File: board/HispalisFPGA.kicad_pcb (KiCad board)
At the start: 4 copper layers, 91.3 x 79.9 mm, 133 parts, among them J1 HC-TYPE-C-16P-01A, Q1 DMG1012T, Q2 DMG1012T, Q3 DMG1012T, Q4 DMG1012T, SW1 SW_DIP_x08, U1 93LC46B, U2 FT2232HQ, Y1 12MHz

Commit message: Add metadata
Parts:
- moved BTN2 52.0 mm to (102.6, 105.6)
- moved C37 52.0 mm to (66.9, 101.7)
- moved C45 52.0 mm to (77.0, 97.5)
- moved DISPLAY1 52.0 mm to (62.7, 128.9)
- moved FLASH1 52.0 mm to (77.0, 97.5)
- moved FPGA1 52.0 mm to (62.5, 102.6)
- moved LD1 52.0 mm to (40.6, 136.1)
- moved LD2 52.0 mm to (45.6, 136.1)
- moved LD3 52.0 mm to (50.6, 136.1)
- moved LD4 52.0 mm to (55.6, 136.1)
- moved LD5 52.0 mm to (60.6, 136.1)
- moved LD6 52.0 mm to (65.6, 136.1)
- moved LD7 52.0 mm to (70.6, 136.1)
- moved LD8 52.0 mm to (75.6, 136.1)
- moved R1 52.0 mm to (92.1, 90.0)
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
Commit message: Add logo
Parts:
- added LOGO1: LOGO, HispalisFPGA:logo, F.Cu at (89.4, 76.8)

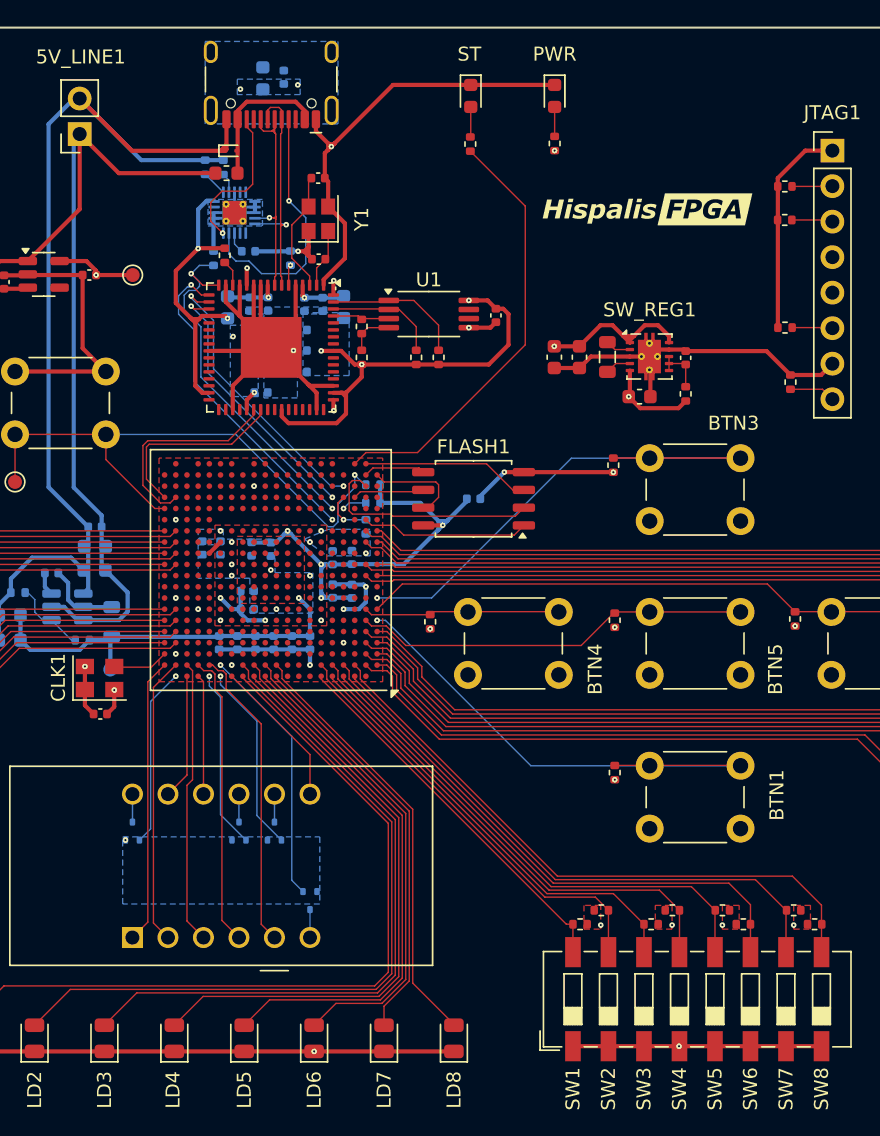
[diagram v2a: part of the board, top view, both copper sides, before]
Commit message: Further adaptations for JLCPCB order
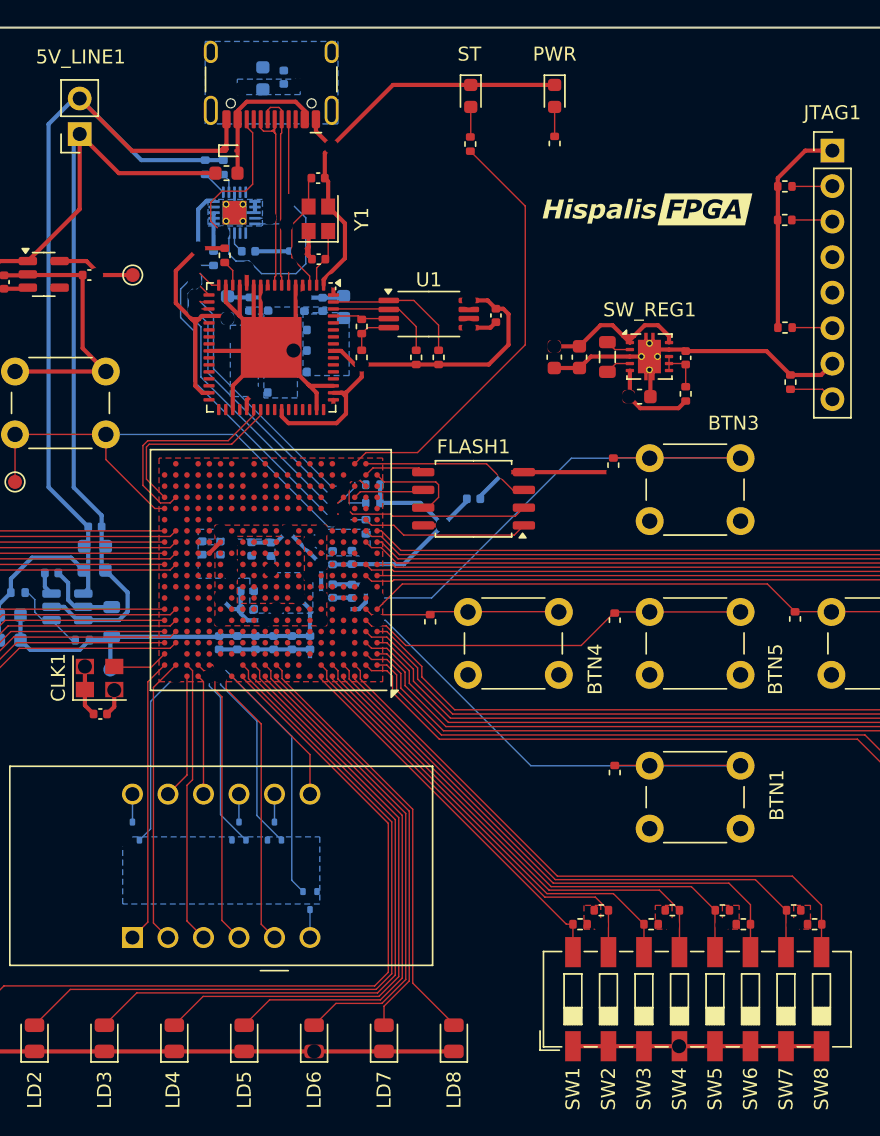
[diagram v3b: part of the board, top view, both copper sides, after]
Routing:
- net GND: track 274.7 -> 272.0 mm
- net TMS: track 67.5 -> 66.8 mm

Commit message: Move logo footprint to the right directory
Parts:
- HISPALISFPGA-LOGO1: renamed from LOGO1; value LOGO -> HISPALISFPGA-LOGO; footprint HispalisFPGA:logo -> HispalisFPGA:HispalisFPGA-Logo
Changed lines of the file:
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@@
 		)
 	)
-	(footprint "HispalisFPGA:logo"
+	(footprint "HispalisFPGA:HispalisFPGA-Logo"
 		(layer "F.Cu")
 		(at 89.4 76.8)
-		(property "Reference" "LOGO1"
+		(property "Reference" "HISPALISFPGA-LOGO1"
 			(at 0 0 0)
 			(layer "F.SilkS")
@@
 			)
 		)
-		(property "Value" "LOGO"
+		(property "Value" "HISPALISFPGA-LOGO"
 			(at 0.75 0 0)
 			(layer "F.SilkS")
@@
 			)
 		)
-		(property "Footprint" "HispalisFPGA:logo"
+		(property "Footprint" "HispalisFPGA:HispalisFPGA-Logo"
 			(at 0 0 0)
 			(layer "F.Fab")
